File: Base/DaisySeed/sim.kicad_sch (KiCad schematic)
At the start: 12 parts

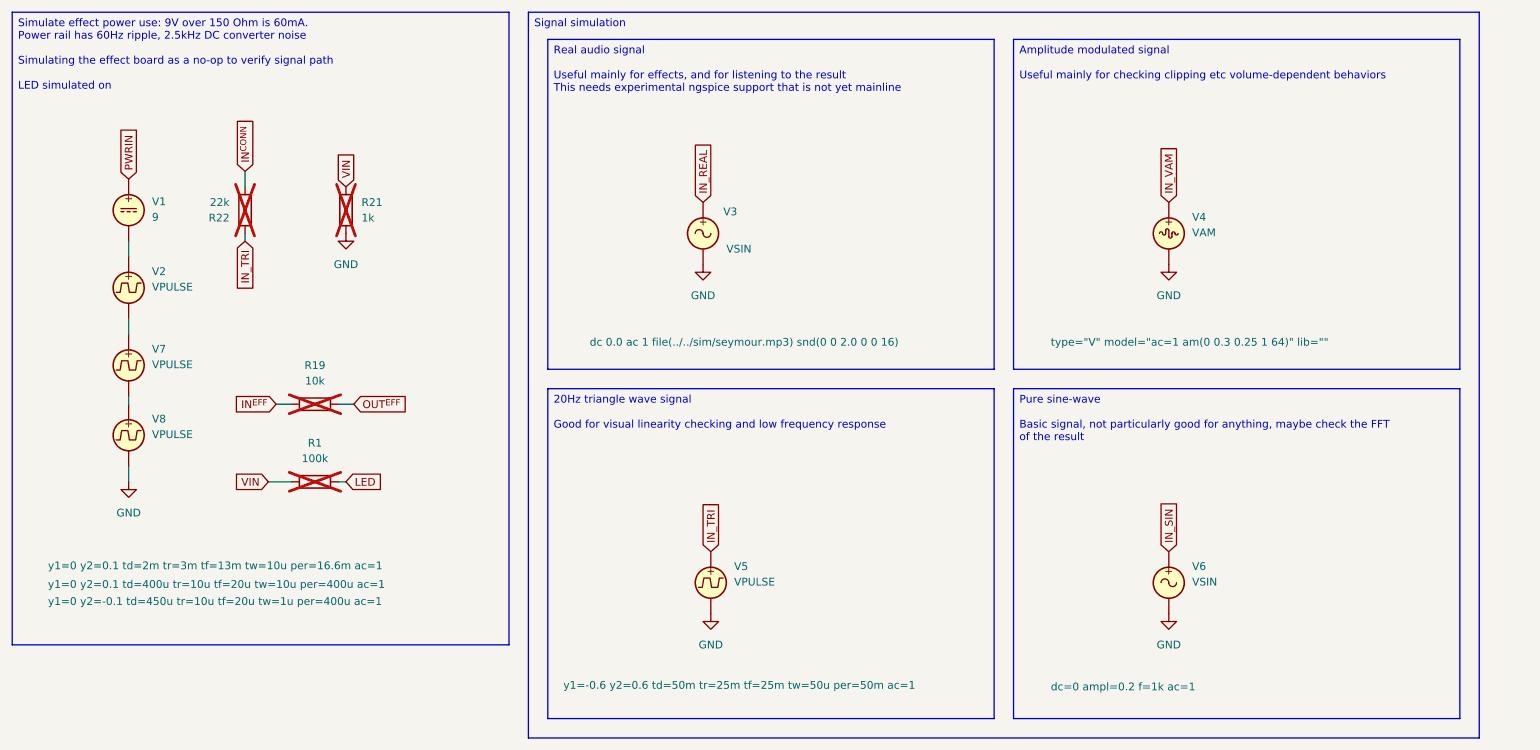
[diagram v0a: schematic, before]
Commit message: Downgrade Daisy Seed boards to kicad v9.0
Since I don't do audio signal simulation with the Daisy Seed boards,
let's try to downcovert to the standard kicad version to make it easier
to use without having to have a self-compiled version.

Kicad doesn't make this particularly easy, I'm afraid.  Let's hope this
didn't do anything bad.  It still simulates, and looks superficially ok.

Signed-off-by: Linus Torvalds <torvalds@linux-foundation.org>
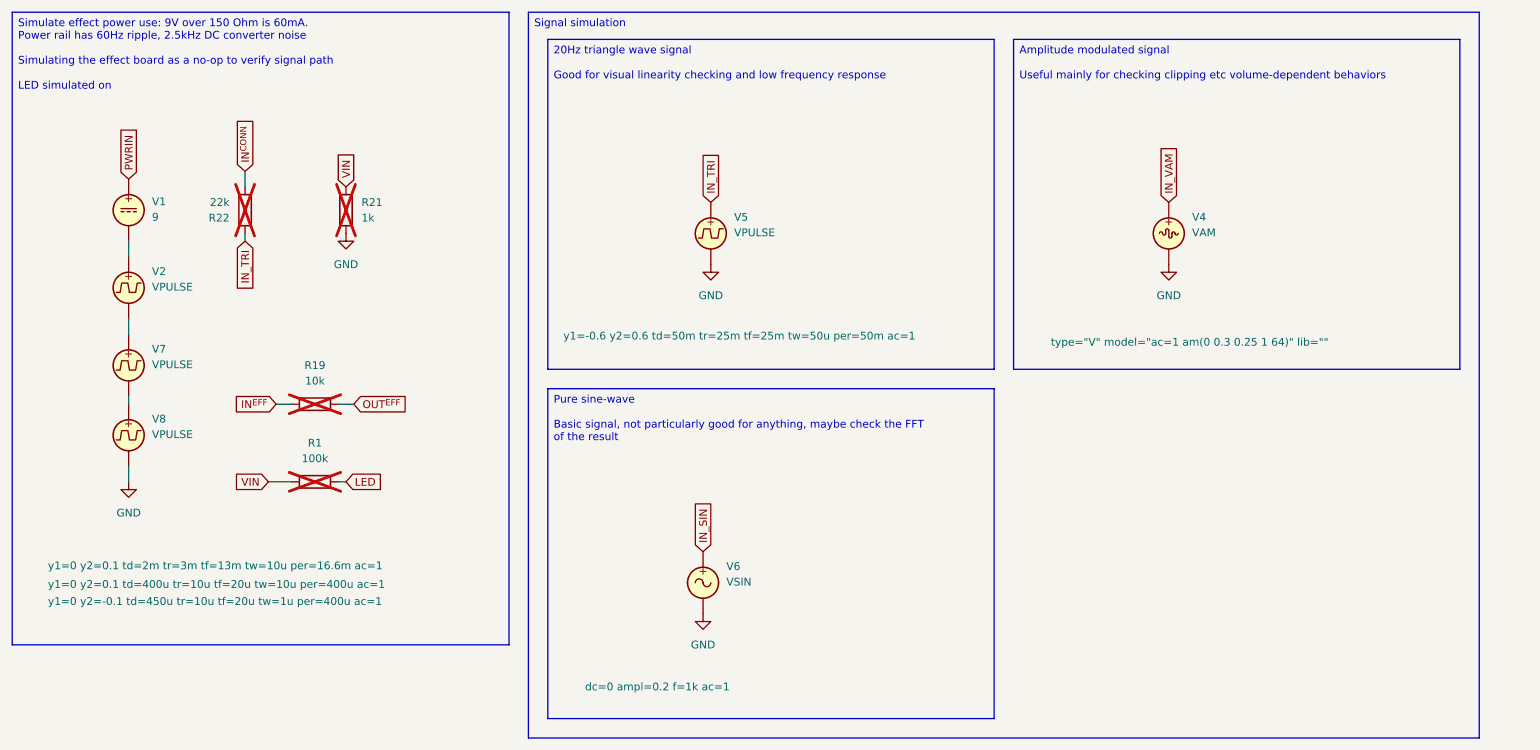
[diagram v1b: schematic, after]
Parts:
- removed V3: VSIN, symbol Simulation_SPICE:VSIN
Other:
- moved on the sheet: V5, V6

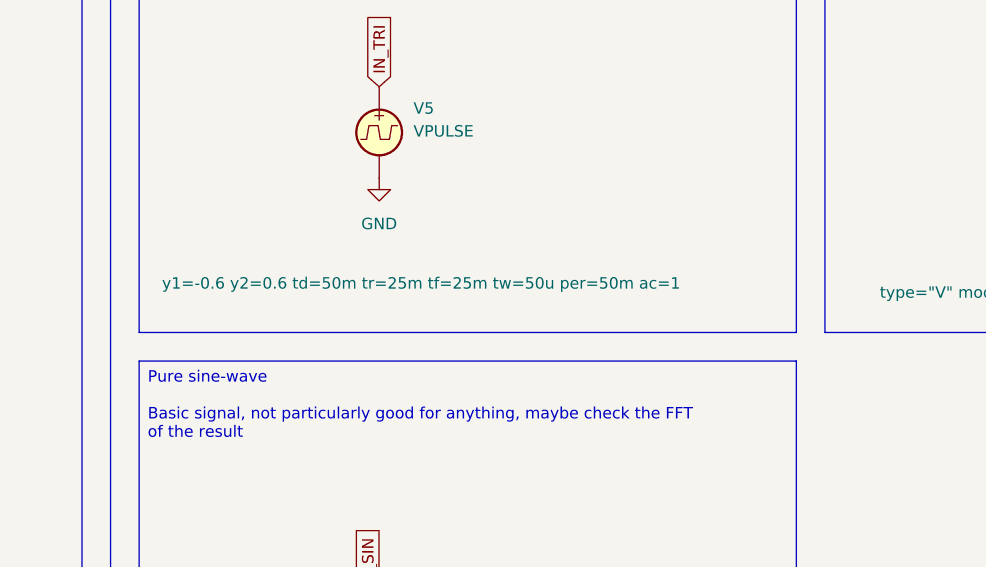
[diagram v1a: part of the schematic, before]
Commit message: Add input signal re-biasing to the Daisy Seed after all
Yes, the Daisy Seed ends up AC-coupling the input, and will re-bias it
to the mid-point of the analog voltage range for the audio codec.

But thinking some more about it, I started worrying about the capacitor
used. In particular, it might very well be a low-voltage one, and the
dual JFET input will have a buffered output voltage in the 5V+ range.

Simulation puts the signal level centered at 7.4V, but who knows what an
actual LS844 will be.  For all I know the dual JFET thing really would
want more of a voltage range than a 9V positive supply and it will not
work very well in real life, but we'll see.

[ I can always go back to the single MMBF5103 as an input buffer, that
  worked fine and is more than sufficient for a guitar pedal -
  particularly one of my design.

  The whole "let's used two matched JFET's" is really me being rather
  silly, after having seen reports of it having particularly good THD by
  Rod Elliott (ESP) [1] and Erno Borbely [2].

  ESP uses the matched JFET as a current source, Erno Borbely as a
  current sink. Mostly it shouldn't make any difference, but I randomly
  did the current sink thing. And that does end up with the signal at a
  higher voltage ]

Regardless, it's entirely possible that the AC coupling on the Daisy
Seed uses a capacitor that is rated for something like 6.3V, which is
common for smaller SMT caps.  That would make sense, since the
assumption is an incoming signal around ground, with the center of the
analog voltage at 1.6V.

So my assumption that the AC coupling of the Daisy Seed would make it
unnecessary to do any AC coupling on the base board signal was clearly
horribly flawed.  Let's fix it.

I wonder what the next horribly flawed idea is?

Link: https://sound-au.com/articles/jfet-design.htm#s5 [1]
Link: https://pearl-hifi.com/06_Lit_Archive/14_Books_Tech_Papers/Borbely_Erno/JFETS_The_New_Frontier.pdf [2]
Signed-off-by: Linus Torvalds <torvalds@linux-foundatio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
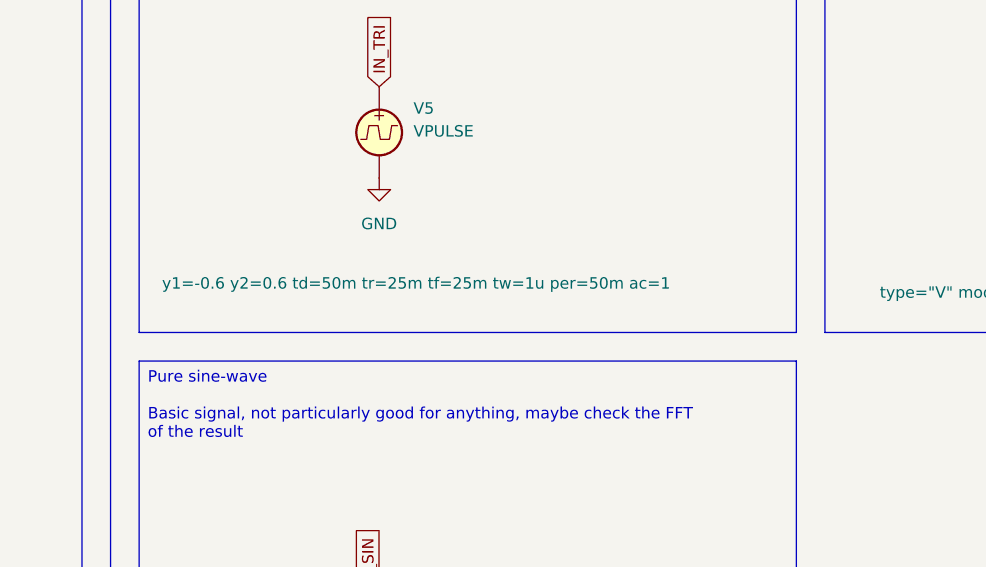
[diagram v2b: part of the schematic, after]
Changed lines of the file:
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@@
 			)
 		)
-		(property "Sim.Params" "y1=-0.6 y2=0.6 td=50m tr=25m tf=25m tw=50u per=50m ac=1"
+		(property "Sim.Params" "y1=-0.6 y2=0.6 td=50m tr=25m tf=25m tw=1u per=50m ac=1"
 			(at 104.14 67.564 0)
 			(effects

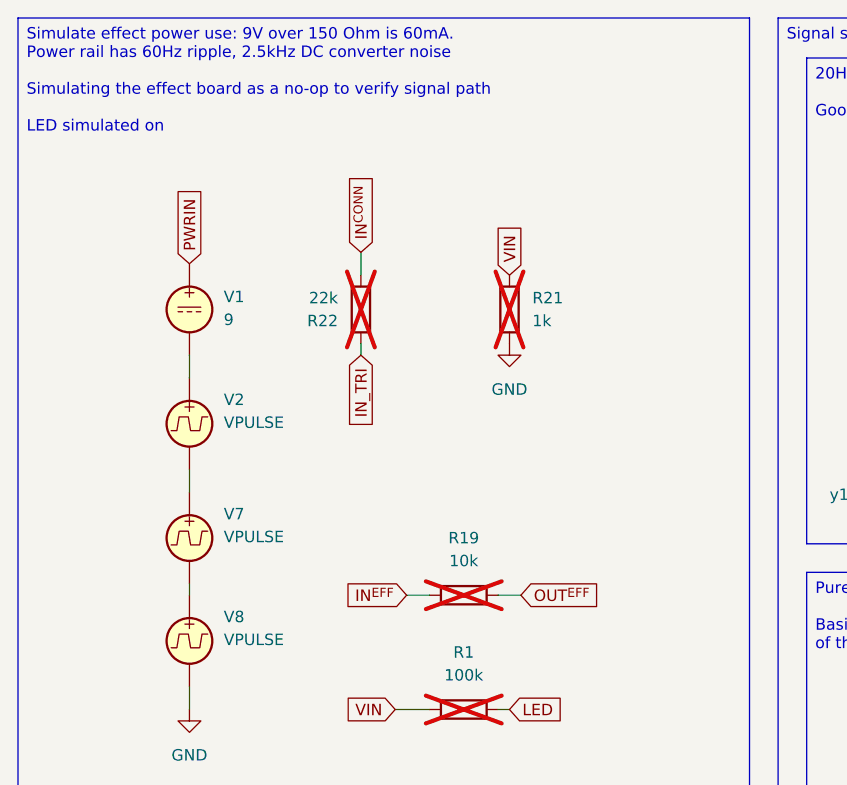
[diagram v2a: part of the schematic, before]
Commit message: Add aggressive low-pass filter to the Daisy Seed base board output
This is from me looking at the HF noise from the Daisy Seed on the
oscilloscope, and then checking what the Hothouse padal looks like.

The Hothouse actually looks really clean - kudos to Ricky Sheaves.  The
reason seems to be a rather aggressive low-pass filter with the 3dB
point at 22kHz.  That will attenuate some of the audio band too, but
looks like it's the right thing to do considering the noise.

(Of course, the Hothouse also does an op-amp to buffer the end result.
My silly discrete component board does not.  That will affect the end
result too, but the output impedance should already be pretty low for a
guitar pedal even without the extra output buffer).

Change the sim to have a simulated 100 Ohm impedance signal output from
the Daisy Seed so that the AC simulation makes sense.  Without that this
just resulted in nonsensical output filtering.

While looking at the AC response, also change the input caps to 4.7uF -
I think that's what I used for the test board, and you definitely want
something bigger than 0.47uF for bass response.

Signed-off-by: Linus Torvalds <torvalds@linux-foundation.org>
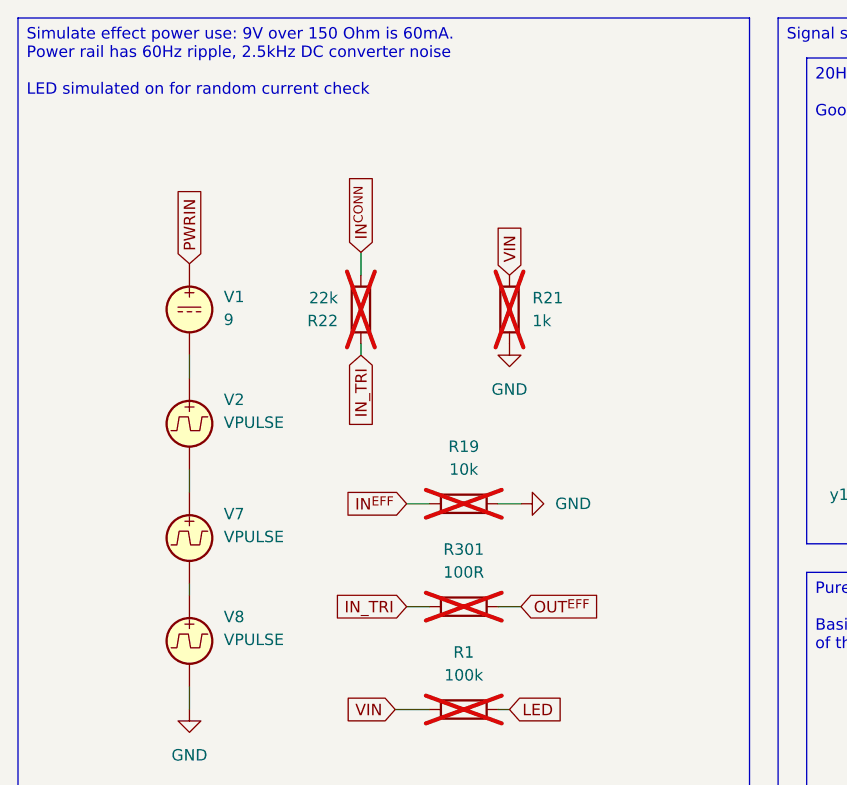
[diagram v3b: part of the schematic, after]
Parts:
- added R301: 100R, symbol Device:R
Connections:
- net GND: now also R19.1
- net IN_TRI: now also R301.2
- net OUT^{EFF}: now also R301.1; no longer R19.1
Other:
- moved on the sheet: R19
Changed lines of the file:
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@@
 		)
 	)
-	(text_box "Simulate effect power use: 9V over 150 Ohm is 60mA.\nPower rail has 60Hz ripple, 2.5kHz DC converter noise\n\nSimulating the effect board as a no-op to verify signal path\n\nLED simulated on"
+	(text_box "Simulate effect power use: 9V over 150 Ohm is 60mA.\nPower rail has 60Hz ripple, 2.5kHz DC converter noise\n\nLED simulated on for random current check"
 		(exclude_from_sim no)
 		(at 13.97 14.605 0)
@@
 	(wire
 		(pts
-			(xy 57.15 78.74) (xy 59.69 78.74)
+			(xy 57.15 80.01) (xy 59.69 80.01)
 		)
 		(stroke
@@
 	(wire
 		(pts
-			(xy 33.02 64.77) (xy 33.02 67.31)
+			(xy 57.15 68.58) (xy 59.69 68.58)
 		)
 		(stroke
@@
 	(wire
 		(pts
-			(xy 33.02 88.9) (xy 33.02 91.44)
+			(xy 33.02 64.77) (xy 33.02 67.31)
 		)
 		(stroke
@@
 	(wire
 		(pts
-			(xy 67.31 78.74) (xy 69.85 78.74)
+			(xy 33.02 88.9) (xy 33.02 91.44)
 		)
 		(stroke
@@
 	(wire
 		(pts
-			(xy 52.07 50.8) (xy 52.07 52.07)
+			(xy 67.31 68.58) (xy 69.85 68.58)
 		)
 		(stroke
@@
 	(wire
 		(pts
-			(xy 33.02 52.07) (xy 33.02 54.61)
+			(xy 52.07 50.8) (xy 52.07 52.07)
 		)
 		(stroke
@@
 	(wire
 		(pts
-			(xy 33.02 77.47) (xy 33.02 78.74)
+			(xy 33.02 52.07) (xy 33.02 54.61)
 		)
 		(stroke
@@
 	(wire
 		(pts
-			(xy 55.88 91.44) (xy 59.69 91.44)
+			(xy 33.02 77.47) (xy 33.02 78.74)
 		)
 		(stroke
@@
 	(wire
 		(pts
-			(xy 52.07 40.64) (xy 52.07 43.18)
+			(xy 55.88 91.44) (xy 59.69 91.44)
 		)
 		(stroke
@@
 	(wire
 		(pts
-			(xy 67.31 91.44) (xy 68.58 91.44)
+			(xy 52.07 40.64) (xy 52.07 43.18)
 		)
 		(stroke
@@
 		)
 	)
+	(wire
+		(pts
+			(xy 67.31 91.44) (xy 68.58 91.44)
+		)
+		(stroke
+			(width 0)
+			(type default)
+		)
+	)
+	(wire
+		(pts
+			(xy 67.31 80.01) (xy 69.85 80.01)
+		)
+		(stroke
+			(width 0)
+			(type default)
+		)
+	)
 	(global_label "IN_TRI"
 		(shape input)
@@
 	(global_label "IN^{EFF}"
 		(shape input)
-		(at 57.15 78.74 180)
+		(at 57.15 68.58 180)
 		(fields_autoplaced yes)
 		(effects
@@
 		)
 		(property "Intersheetrefs" "${INTERSHEET_REFS}"
-			(at 49.5177 78.74 0)
+			(at 49.5177 68.58 0)
 			(effects
 				(font
@@
 	(global_label "OUT^{EFF}"
 		(shape input)
-		(at 69.85 78.74 0)
+		(at 69.85 80.01 0)
 		(fields_autoplaced yes)
 		(effects
@@
 		)
 		(property "Intersheetrefs" "${INTERSHEET_REFS}"
-			(at 79.1756 78.74 0)
+			(at 79.1756 80.01 0)
 			(effects
 				(font
@@
 				)
 				(justify left)
+				(hide yes)
+			)
+		)
+	)
+	(global_label "IN_TRI"
+		(shape input)
+		(at 57.15 80.01 180)
+		(fields_autoplaced yes)
+		(effects
+			(font
+				(size 1.27 1.27)
+			)
+			(justify right)
+		)
+		(property "Intersheetrefs" "${INTERSHEET_REFS}"
+			(at 48.4195 80.01 0)
+			(effects
+				(font
+					(size 1.27 1.27)
+				)
+				(justify right)
 				(hide yes)
 			)
@@
 	)
 	(symbol
+		(lib_id "power:GND")
+		(at 69.85 68.58 90)
+		(unit 1)
+		(exclude_from_sim no)
+		(in_bom yes)
+		(on_board yes)
+		(dnp no)
+		(fields_autoplaced yes)
+		(property "Reference" "#PWR0301"
+			(at 76.2 68.58 0)
+			(effects
+				(font
+					(size 1.27 1.27)
+				)
+				(hide yes)
+			)
+		)
+		(property "Value" "GND"
+			(at 73.66 68.5799 90)
+			(effects
+				(font
+					(size 1.27 1.27)
+				)
+				(justify right)
+			)
+		)
+		(property "Footprint" ""
+			(at 69.85 68.58 0)
+			(effects
+				(font
+					(size 1.27 1.27)
+				)
+				(hide yes)
+			)
+		)
+		(property "Datasheet" ""
+			(at 69.85 68.58 0)
+			(effects
+				(font
+					(size 1.27 1.27)
+				)
+				(hide yes)
+			)
+		)
+		(property "Description" "Power symbol creates a global label with name \"GND\" , ground"
+			(at 69.85 68.58 0)
+			(effects
+				(font
+					(size 1.27 1.27)
+				)
+				(hide yes)
+			)
+		)
+		(pin "1"
+		)
+		(instances
+			(project "DaisySeed"
+				(path "/9e337e0b-885b-4d2b-99a2-62cdd082c615/a1084b87-85fd-4b63-8fe4-8749c999d338"
+					(reference "#PWR0301")
+					(unit 1)
+				)
+			)
+		)
+	)
+	(symbol
 		(lib_id "Simulation_SPICE:VPULSE")
 		(at 128.27 50.8 0)
@@
 	(symbol
 		(lib_id "Device:R")
-		(at 63.5 78.74 270)
+		(at 63.5 68.58 270)
 		(unit 1)
 		(exclude_from_sim no)
@@
 		(fields_autoplaced yes)
 		(property "Reference" "R19"
-			(at 63.5 72.39 90)
+			(at 63.5 62.23 90)
 			(effects
 				(font
@@
 		)
 		(property "Value" "10k"
-			(at 63.5 74.93 90)
+			(at 63.5 64.77 90)
 			(effects
 				(font
@@
 		)
 		(property "Footprint" ""
-			(at 63.5 76.962 90)
+			(at 63.5 66.802 90)
 			(effects
 				(font
@@
 		)
 		(property "Datasheet" "~"
-			(at 63.5 78.74 0)
+			(at 63.5 68.58 0)
 			(effects
 				(font
@@
 		)
 		(property "Description" "Resistor"
-			(at 63.5 78.74 0)
+			(at 63.5 68.58 0)
 			(effects
 				(font
@@
 					(unit 1)
 				)
+			)
+		)
+	)
+	(symbol
+		(lib_id "Device:R")
+		(at 63.5 80.01 270)
+		(unit 1)
+		(exclude_from_sim no)
+		(in_bom no)
+		(on_board no)
+		(dnp yes)
+		(fields_autoplaced yes)
+		(property "Reference" "R301"
+			(at 63.5 73.66 90)
+			(effects
+				(font
+					(size 1.27 1.27)
+				)
+			)
+		)
+		(property "Value" "100R"
+			(at 63.5 76.2 90)
+			(effects
+				(font
+					(size 1.27 1.27)
+				)
+			)
+		)
+		(property "Footprint" ""
+			(at 63.5 78.232 90)
+			(effects
+				(font
+					(size 1.27 1.27)
+				)
+				(hide yes)
+			)
+		)
+		(property "Datasheet" "~"
+			(at 63.5 80.01 0)
+			(effects
+				(font
+					(size 1.27 1.27)
+				)
+				(hide yes)
+			)
+		)
+		(property "Description" "Resistor"
+			(at 63.5 80.01 0)
+			(effects
+				(font
+					(size 1.27 1.27)
+				)
+				(hide yes)
+			)
+		)
+		(pin "1"
+		)
+		(pin "2"
+		)
+		(instances
+			(project "DaisySeed"
+				(path "/9e337e0b-885b-4d2b-99a2-62cdd082c615/a1084b87-85fd-4b63-8fe4-8749c999d338"
+					(reference "R301")
+					(unit 1)
+				)
